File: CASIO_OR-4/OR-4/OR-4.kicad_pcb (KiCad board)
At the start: 2 copper layers, 23 x 39.7 mm, 10 parts

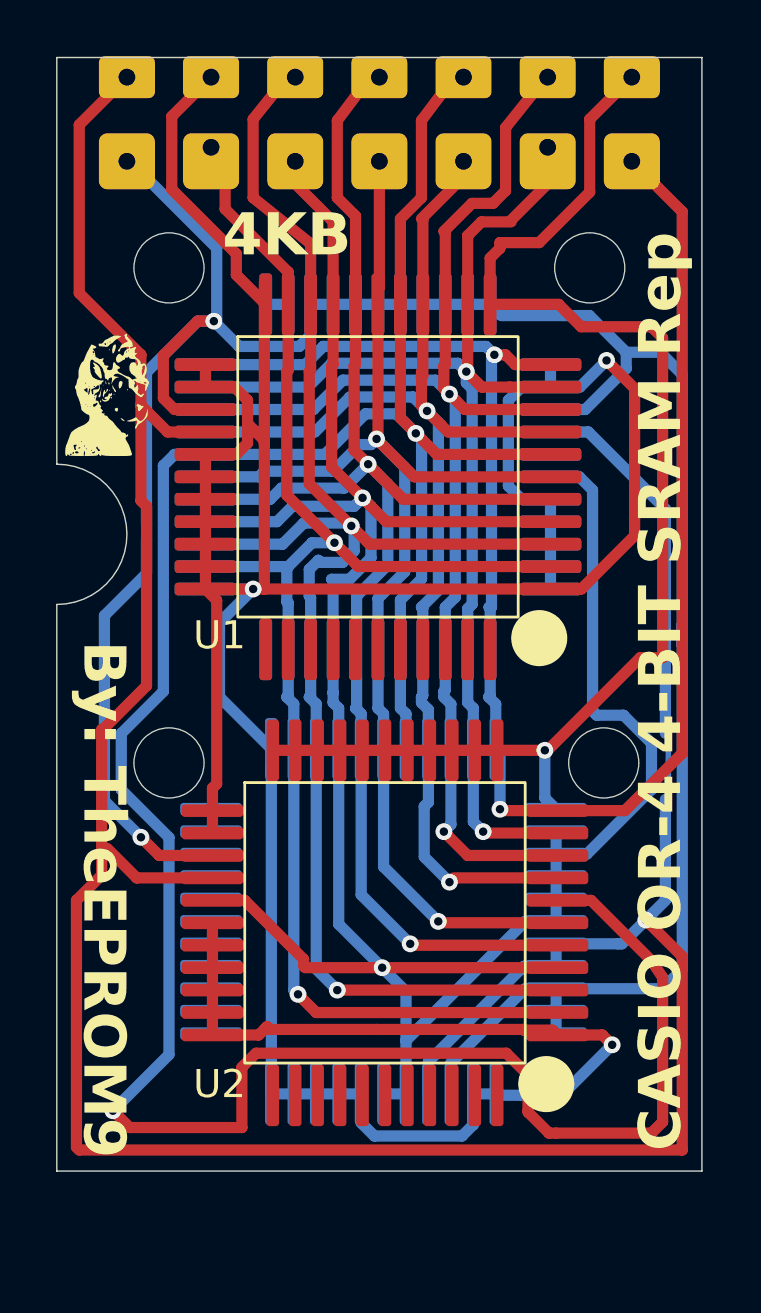
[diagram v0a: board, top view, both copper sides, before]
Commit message: Updated Hole Spaceing
Bottom holes were incorrect.
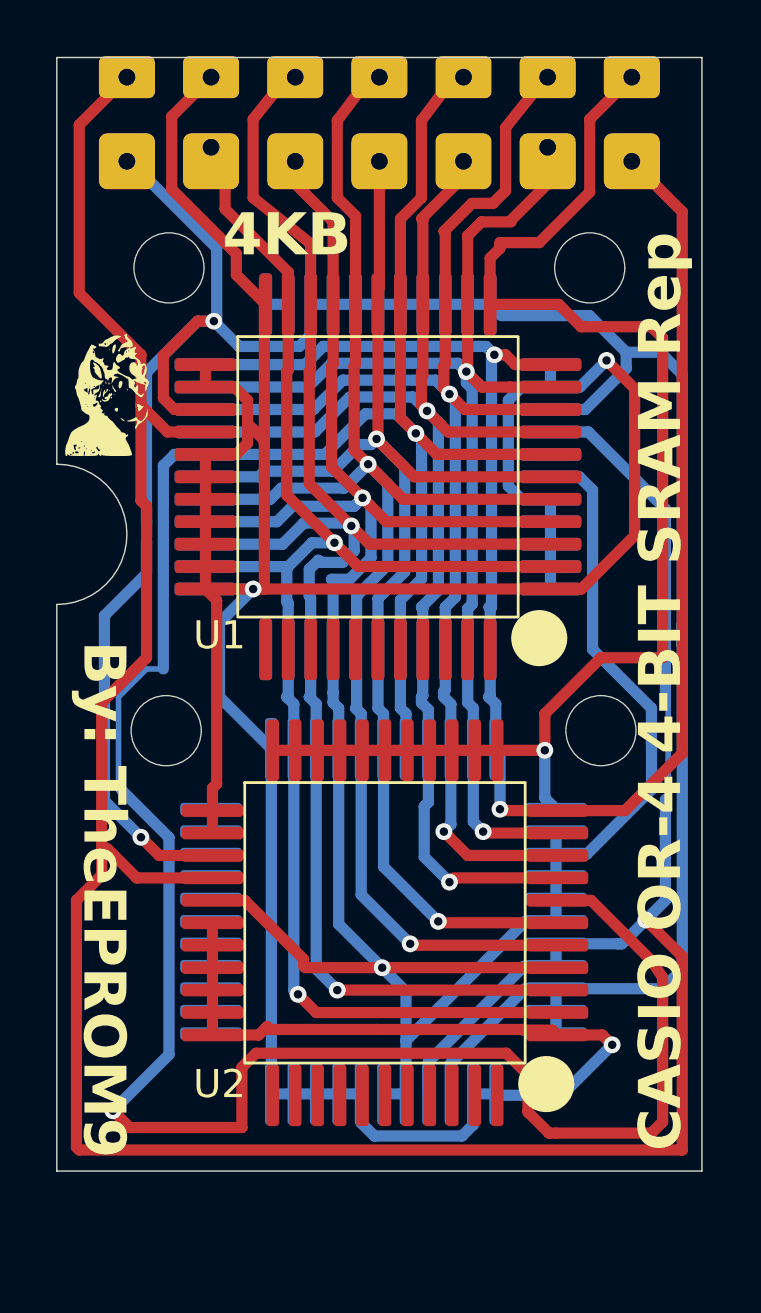
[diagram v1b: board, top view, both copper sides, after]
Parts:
- moved REF** 1.15 mm to (103.9, 84.0)
- moved REF** 1.15 mm to (119.4, 84.0)
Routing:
- net Net-(J1-V3): track 106.9 -> 105.4 mm
- net Net-(J1-INT): track 47.4 -> 48.2 mm
- net Net-(J1-VDD2): track 89.5 -> 88.9 mm
